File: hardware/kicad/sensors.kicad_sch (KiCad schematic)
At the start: 6 parts, among them J3 JST SM06B-GHS-TB (SEN66-SIN-T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, J4 1x5 P1.27mm through-hole head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, U4 MIKROE-2462 NFC Tag 2 Click (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

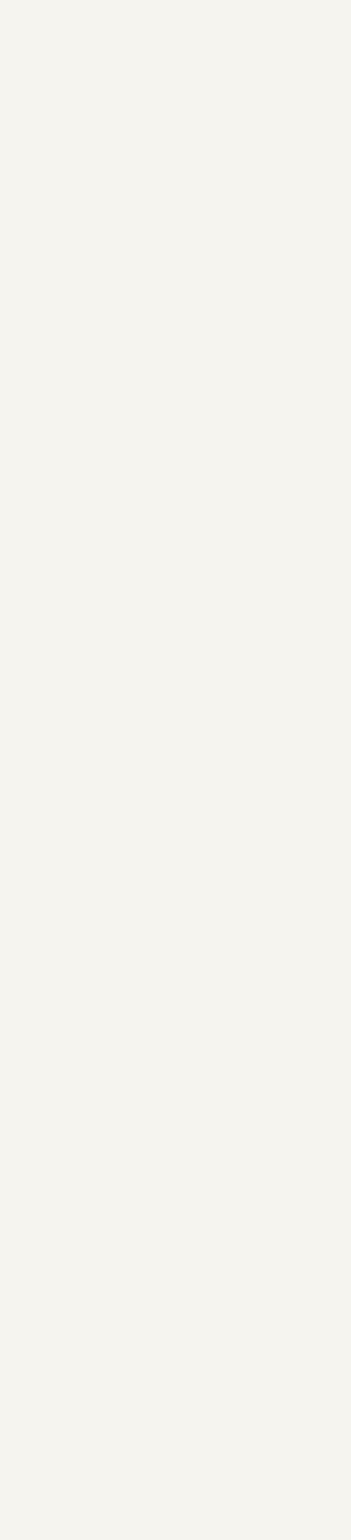
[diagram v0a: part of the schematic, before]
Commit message: kicad+docs: v0.16 - AQI status LED ring (12 x SK6812-SIDE) + resolve OPEN ISSUE #2
Builds the side-emit RGB halo around the central cable hole: 12 SK6812 SIDE-A
LEDs on a Ø22 mm pitch circle (PCB origin = cable hole centre), each oriented
to emit radially OUTWARD into the AK-N-94 perforated cover. Per
hardware/components/_research-led-diffuse-ring.md the side-emit geometry
eliminates the "dot through perforation" problem at the structural level —
the cover never sees the die in line-of-sight.

Pinout verified twice (Normand SK6812 SIDE-A 2018 rev 01 + OPSCO SK6812
SIDE-A-001 2021 rev A/1, both via WebFetch + pdftotext): 1=DIN, 2=VDD,
3=DOUT, 4=GND. This differs from KiCad's stock LED:SK6812 symbol (which
is the PLCC4 5050 variant with 1=VSS/2=DIN/3=VDD/4=DOUT) — OAS ships its
own OAS:SK6812-SIDE symbol and oas:SK6812-SIDE footprint to avoid that
pitfall. Full part spec in hardware/components/sk6812-side.md.

Schematic additions (sensors.kicad_sch):
- 12 × D11..D22 OAS:SK6812-SIDE instances + 12 × C20..C31 Device:C 100 nF
  decoupling caps, vertical stack at X=40.64 with 25.4 mm row pitch.
- Daisy chain DIN→DOUT via 5-segment L-routes that bypass each LED body
  (avoids the spurious DIN↔DOUT short that a horizontal pass-through
  wire would create).
- D11 DIN driven from the new WS2812_DIN hierarchical label.
- D22 DOUT terminated with a no_connect.

Schematic / inter-sheet plumbing:
- mcu.kicad_sch: GPIO 8 (J1.9) moved from no-connect to signal pins.
  New WS2812_DIN hier label on the LEFT edge at the GPIO 8 pin row.
- SUBSHEET_PINS adds WS2812_DIN on the MCU and Sensors LEFT edges.
- Root sheet adds an inter-sheet wire at X = 41.91 (one grid step west
  of the existing NFC_FD vertical) joining the two new sheet pins.

PCB additions (oas.kicad_pcb):
- 12 × SK6812-SIDE footprints placed at θ = 0°..330° (30° steps) on the
  Ø22 mm pitch circle, each rotated to (270 - θ) so its body-local -Y
  (emission face) points radially outward.
- 12 × 100 nF 0402 caps, placed rad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
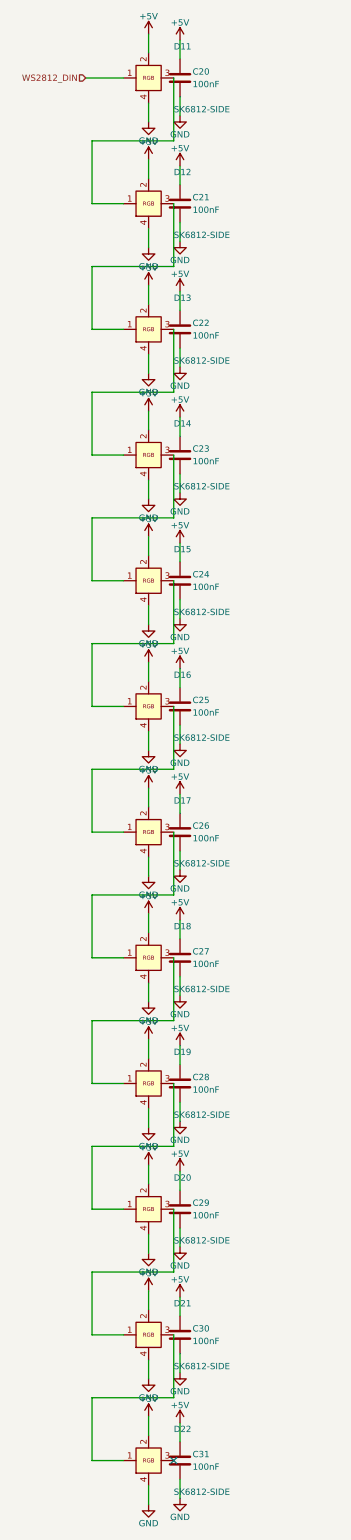
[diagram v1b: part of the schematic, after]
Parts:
- added C20, C21, C22, C23, C24, C25, C26, C27, C28, C29, C30, C31: 100nF, symbol Device:C
- added D11, D12, D13, D14, D15, D16, D17, D18, D19, D20, D21, D22: SK6812-SIDE, oas:SK6812-SIDE, symbol OAS:SK6812-SIDE
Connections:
- net +5V: now also C20.1, C21.1, C22.1, C23.1, C24.1, C25.1, C26.1, C27.1, C28.1, C29.1, C30.1, C31.1, D11.2 (VDD), D12.2 (VDD), D13.2 (VDD), D14.2 (VDD), D15.2 (VDD), D16.2 (VDD), D17.2 (VDD), D18.2 (VDD), D19.2 (VDD), D20.2 (VDD), D21.2 (VDD), D22.2 (VDD)
- net GND: now also C20.2, C21.2, C22.2, C23.2, C24.2, C25.2, C26.2, C27.2, C28.2, C29.2, C30.2, C31.2, D11.4 (GND), D12.4 (GND), D13.4 (GND), D14.4 (GND), D15.4 (GND), D16.4 (GND), D17.4 (GND), D18.4 (GND), D19.4 (GND), D20.4 (GND), D21.4 (GND), D22.4 (GND)
- new net: D18.3 (DOUT), D19.1 (DIN)
- new net: D19.3 (DOUT), D20.1 (DIN)
- new net: D16.3 (DOUT), D17.1 (DIN)
- new net: D17.3 (DOUT), D18.1 (DIN)
- new net: D11.3 (DOUT), D12.1 (DIN)
- new net: D20.3 (DOUT), D21.1 (DIN)
- new net: D12.3 (DOUT), D13.1 (DIN)
- new net: D21.3 (DOUT), D22.1 (DIN)
- new net: D13.3 (DOUT), D14.1 (DIN)
- new net: D14.3 (DOUT), D15.1 (DIN)
- new net: D15.3 (DOUT), D16.1 (DIN)
- new net WS2812_DIN: D11.1 (DIN)
- no-connect marks 10 -> 11

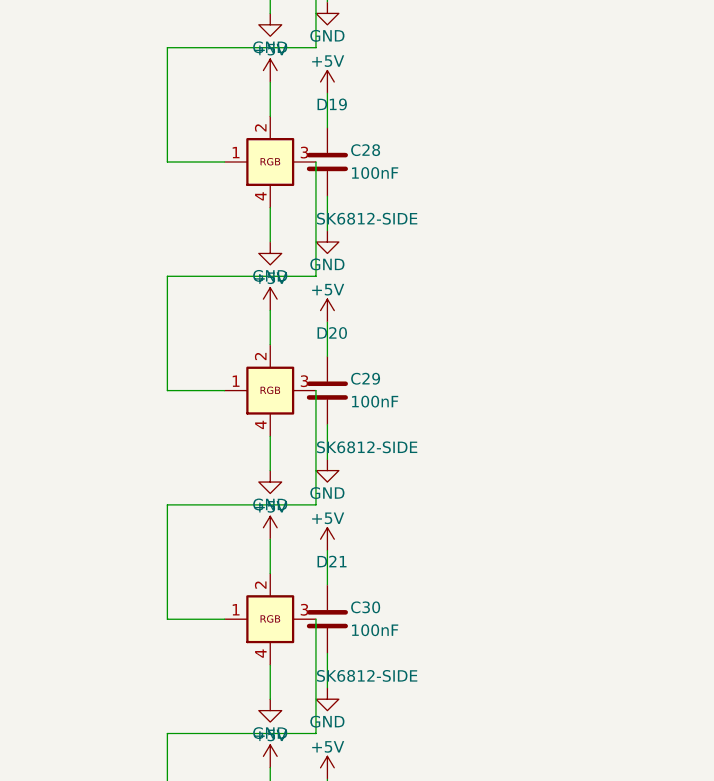
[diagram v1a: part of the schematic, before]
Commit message: kicad+docs: v0.17 - J1 24V terminal block placed at central cable-hole zone
Relocate J1 (Phoenix MSTBA 2,5/3-G-5,08) from the chord-edge connector
strip into the central PCB area, directly north of the Ø12 mm cable
pass-through hole. Removes one LED (D20) + its decoupling cap (C29)
from the AQI ring to open a corridor for the 24 V supply cable.

Geometry:
  - J1 PCB anchor (-5.08, -22.4), rotation 0.
  - Pin row at PCB Y=-22.4, pin 1=+24V at X=-5.08, pin 2=GND at X=0,
    pin 3=PE at X=+5.08. Body extends south to PCB Y=-12.29.
  - Cable enters connector mouth from south face; ~6.3-6.6 mm of
    horizontal travel for the cable bend from the hole exit.
  - ESP32 anchor_y shifted -24.70 -> -26.20 (1.5 mm north) to make
    room for J1's 13 mm courtyard depth between the LED ring's north
    corners and the ESP32 daughterboard's south edge.

LED ring v0.17 changes:
  - LED_RING_SKIP_INDICES = (9,) skips D20 in both PCB and schematic.
  - Daisy chain: D19.DOUT -> D21.DIN (5-segment route through the now-
    empty D20 row position in the schematic column).
  - Final ring has 11 LEDs (was 12 in v0.16).

PCB silkscreen:
  - "J1 (24V)" board-level F.SilkS label 6 mm west of the J1 body.
  - "24V"/"GND"/"PE" per-pin labels on F.Fab (silk-overlap-exempt).
  - In-footprint Reference/Value hidden to avoid silk_overlap with
    the ESP32 daughterboard south edge.

Schematic:
  - J1's Footprint property populated (was empty in v0.2). Datasheet
    and Description also filled in.
  - D20 + C29 schematic symbols and per-LED wires dropped.

DRC=0, ERC=0.

Co-Authored-By: Claude Opus 4.7 (1M context) <noreply@anthropic.com>
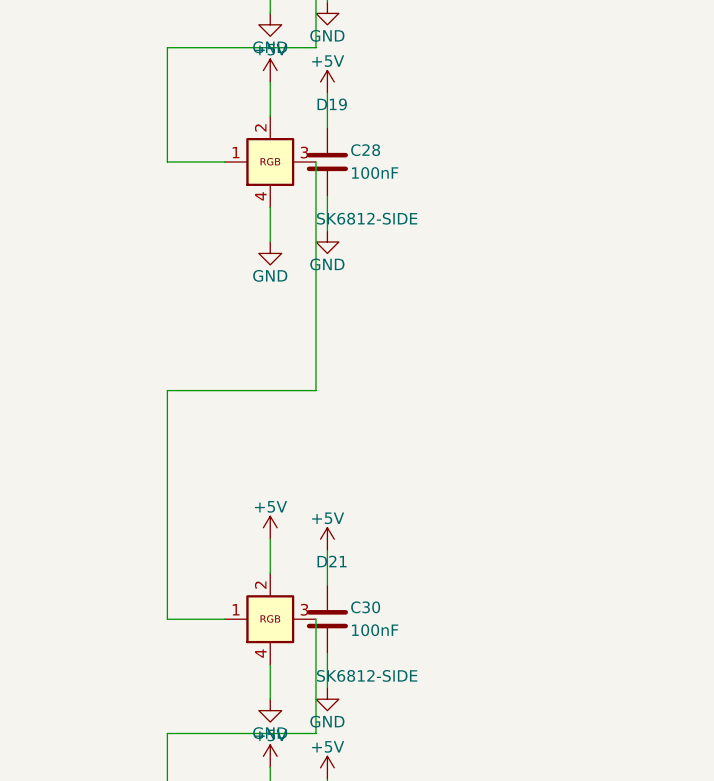
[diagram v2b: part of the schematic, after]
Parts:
- removed C29: 100nF, symbol Device:C
- removed D20: SK6812-SIDE, oas:SK6812-SIDE, symbol OAS:SK6812-SIDE
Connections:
- net at D19.3 (DOUT): now also D21.1 (DIN)

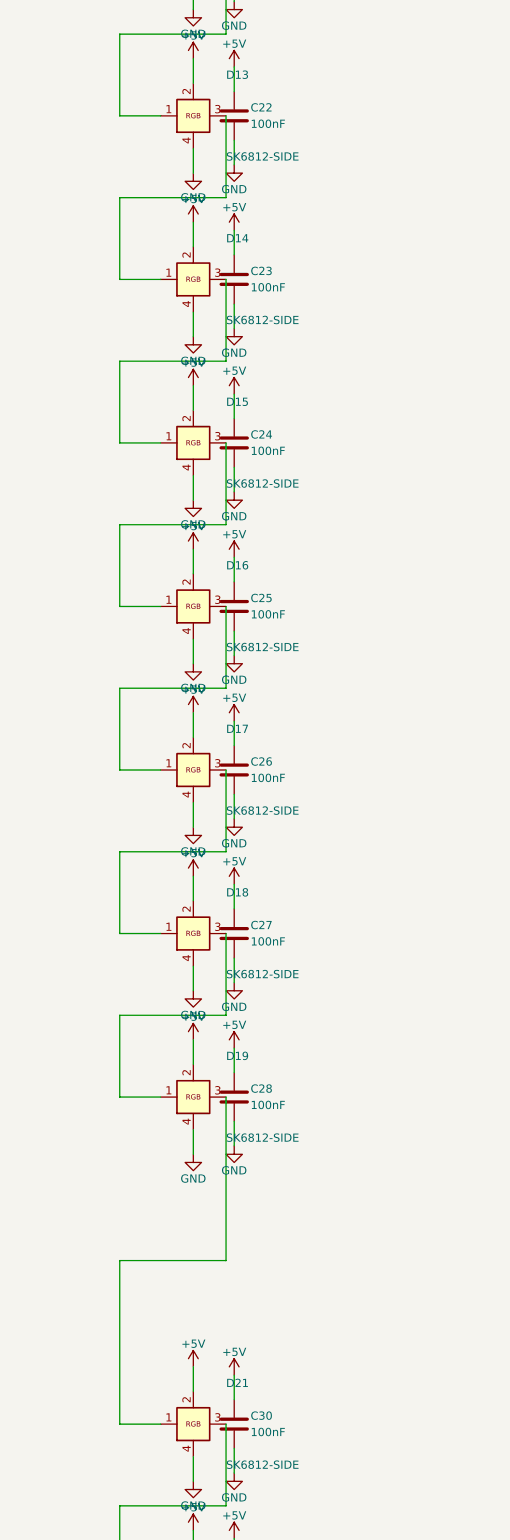
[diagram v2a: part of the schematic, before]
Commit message: kicad+docs: v0.18 - flip J1 24V terminal block from north to south of cable hole
User decision to relocate J1 to the south side (more open clearance:
ESP32 occupies the north, the south corridor between the cable hole
and the chord cutouts is largely empty). v0.17's tight ESP32 shift and
sub-1 mm PCB outline clearance are no longer needed.

LED ring:
  - LED_RING_SKIP_INDICES changed from (9,) to (3,).
  - D14 + C23 removed (replaces D20 + C29 removal from v0.17).
  - D20 + C29 restored to their v0.16 placement.
  - Daisy chain: D13.DOUT -> D15.DIN (mirror of v0.17's D19->D21).

J1 PCB placement:
  - Anchor (+5.08, +22.4), rotation 180.
  - Pin row at PCB Y=+22.4, pin 1 (+24V) at X=+5.08, pin 2 (GND) at
    X=0, pin 3 (PE) at X=-5.08.
  - Body extends north to PCB Y=+12.29 (cable entry face), facing
    the cable hole's south edge at Y=+6.
  - Effective cable bend travel: 6.29 mm (same magnitude as v0.17
    north placement; mirror geometry).

ESP32 anchor_y reverted from -26.20 (v0.17) -> -24.70 (v0.15.3 value).
PCB outline clearance restored from 1.41 mm to 2.73 mm.

Clearances (v0.18):
  - LED ring D13/D15 south corners: 0.23 mm courtyard, 0.62 mm F.SilkS
  - C3 cutout north edge: 4.10 mm courtyard
  - SEN66 body west edge: 14.38 mm X
  - J3 SEN66 socket west edge: 20.90 mm X
  - Zip-tie hole ZT1: 11.77 mm X, no Y conflict

Silk labels:
  - "J1 (24V)" board-level label moved from west to east of J1
    (PCB (+15, +22.4)) because MIKROE-2462 body silk occupies the
    west side at this Y. East side has 14.77 mm clear strip.
  - Per-pin F.Fab labels at PCB Y = pin_y - 0.8 (north of pin row),
    with X order reversed to match new pin layout (24V east, PE west).

DRC=0, ERC=0.

Co-Authored-By: Claude Opus 4.7 (1M context) <noreply@anthropic.com>
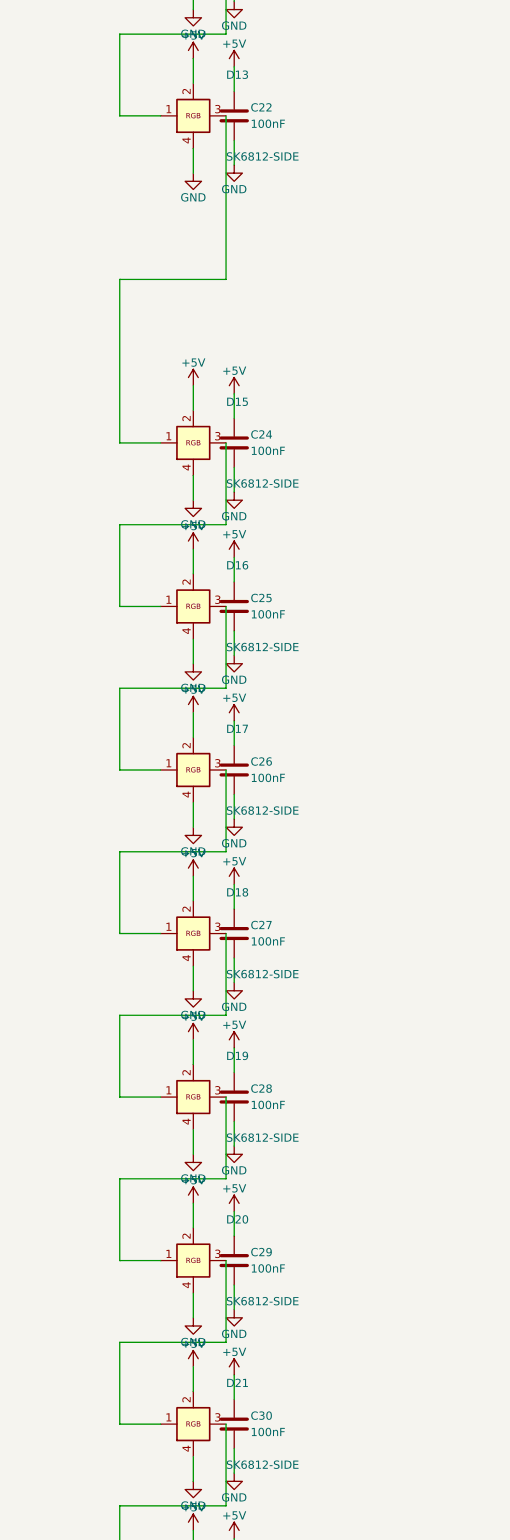
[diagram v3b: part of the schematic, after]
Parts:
- removed C23: 100nF, symbol Device:C
- removed D14: SK6812-SIDE, oas:SK6812-SIDE, symbol OAS:SK6812-SIDE
- added C29: 100nF, symbol Device:C
- added D20: SK6812-SIDE, oas:SK6812-SIDE, symbol OAS:SK6812-SIDE
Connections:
- net +5V: now also C29.1, D20.2 (VDD)
- net GND: now also C29.2, D20.4 (GND)
- net at D19.3 (DOUT): now also D20.1 (DIN); no longer D21.1 (DIN)
- net at D13.3 (DOUT): now also D15.1 (DIN)
- new net: D20.3 (DOUT), D21.1 (DIN)
